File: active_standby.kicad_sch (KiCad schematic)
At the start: 13 parts, among them Q2 BSS138, U24 SN3257QDYYRQ1, U30 SN3257QDYYRQ1

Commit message: Add OTHER\_HW\_POWER\_N to a GPIO
So in the externally driven active/standby case the other power state
can be monitored.

Also fix issues in the processor pin list.

Signed-off-by: Corey Minyard <corey@minyard.net>
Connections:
- net OTHER_HW_POWER_OFF_N: now reaches Q2.3 (D), U30.12 (D4)
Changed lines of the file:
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@@
+	)
+	(junction
+		(at 130.81 148.59)
+		(diameter 0)
+		(color 0 0 0 0)
 	)
 	(junction
@@
 	(wire
 		(pts
+			(xy 130.81 148.59) (xy 135.89 148.59)
+		)
+		(stroke
+			(width 0)
+			(type default)
+		)
+	)
+	(wire
+		(pts
 			(xy 69.85 135.89) (xy 62.23 135.89)
 		)
@@
 				(hide yes)
 			)
+		)
+	)
+	(global_label "OTHER_HW_POWER_OFF_N"
+		(shape input)
+		(at 135.89 148.59 0)
+		(fields_autoplaced yes)
+		(effects
+			(font
+				(size 1.524 1.524)
+			)
+			(justify left)
+		)
+		(property "Intersheetrefs" "${INTERSHEET_REFS}"
+			(at 167.4977 148.59 0)
+			(effects
+				(font
+					(size 1.27 1.27)
+				)
+				(justify left)
+				(hide yes)
+			)

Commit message: Change a transistor to a SOT-523
Save some space

Signed-off-by: Corey Minyard <corey@minyard.net>
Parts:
- Q2: footprint Package_TO_SOT_SMD:SOT-23 -> Package_TO_SOT_SMD:SOT-523
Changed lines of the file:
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@@
 			)
 		)
-		(property "Footprint" "Package_TO_SOT_SMD:SOT-23"
+		(property "Footprint" "Package_TO_SOT_SMD:SOT-523"
 			(at 128.27 170.815 0)
 			(effects

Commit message: Convert a lot of parts to 0402
The passives across the top where things are crowded.

Signed-off-by: Corey Minyard <corey@minyard.net>
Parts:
- R101, R102, R103, R108, R113, R91, R92, R93, R94, R95: footprint Resistor_SMD:R_0603_1608Metric_Pad0.98x0.95mm_HandSolder -> Resistor_SMD:R_0402_1005Metric_Pad0.72x0.64mm_HandSolder
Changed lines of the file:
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@@
 			)
 		)
-		(property "Footprint" "Resistor_SMD:R_0603_1608Metric_Pad0.98x0.95mm_HandSolder"
+		(property "Footprint" "Resistor_SMD:R_0402_1005Metric_Pad0.72x0.64mm_HandSolder"
 			(at 236.982 73.66 90)
 			(effects
@@
 			)
 		)
-		(property "Footprint" "Resistor_SMD:R_0603_1608Metric_Pad0.98x0.95mm_HandSolder"
+		(property "Footprint" "Resistor_SMD:R_0402_1005Metric_Pad0.72x0.64mm_HandSolder"
 			(at 236.982 142.24 90)
 			(effects
@@
 			)
 		)
-		(property "Footprint" "Resistor_SMD:R_0603_1608Metric_Pad0.98x0.95mm_HandSolder"
+		(property "Footprint" "Resistor_SMD:R_0402_1005Metric_Pad0.72x0.64mm_HandSolder"
 			(at 169.672 114.3 90)
 			(effects
@@
 			)
 		)
-		(property "Footprint" "Resistor_SMD:R_0603_1608Metric_Pad0.98x0.95mm_HandSolder"
+		(property "Footprint" "Resistor_SMD:R_0402_1005Metric_Pad0.72x0.64mm_HandSolder"
 			(at 236.982 127 90)
 			(effects
@@
 			)
 		)
-		(property "Footprint" "Resistor_SMD:R_0603_1608Metric_Pad0.98x0.95mm_HandSolder"
+		(property "Footprint" "Resistor_SMD:R_0402_1005Metric_Pad0.72x0.64mm_HandSolder"
 			(at 139.192 176.53 90)
 			(effects
@@
 			)
 		)
-		(property "Footprint" "Resistor_SMD:R_0603_1608Metric_Pad0.98x0.95mm_HandSolder"
+		(property "Footprint" "Resistor_SMD:R_0402_1005Metric_Pad0.72x0.64mm_HandSolder"
 			(at 169.672 134.62 90)
 			(effects
@@
 			)
 		)
-		(property "Footprint" "Resistor_SMD:R_0603_1608Metric_Pad0.98x0.95mm_HandSolder"
+		(property "Footprint" "Resistor_SMD:R_0402_1005Metric_Pad0.72x0.64mm_HandSolder"
 			(at 132.842 33.02 90)
 			(effects
@@
 			)
 		)
-		(property "Footprint" "Resistor_SMD:R_0603_1608Metric_Pad0.98x0.95mm_HandSolder"
+		(property "Footprint" "Resistor_SMD:R_0402_1005Metric_Pad0.72x0.64mm_HandSolder"
 			(at 236.982 88.9 90)
 			(effects
@@
 			)
 		)
-		(property "Footprint" "Resistor_SMD:R_0603_1608Metric_Pad0.98x0.95mm_HandSolder"
+		(property "Footprint" "Resistor_SMD:R_0402_1005Metric_Pad0.72x0.64mm_HandSolder"
 			(at 132.842 111.76 90)
 			(effects
@@
 			)
 		)
-		(property "Footprint" "Resistor_SMD:R_0603_1608Metric_Pad0.98x0.95mm_HandSolder"
+		(property "Footprint" "Resistor_SMD:R_0402_1005Metric_Pad0.72x0.64mm_HandSolder"
 			(at 170.942 71.12 90)
 			(effects

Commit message: Add a current limiter for on-board +5V devices
Signed-off-by: Corey Minyard <corey@minyard.net>
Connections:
- net VSYS renamed +5VAL

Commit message: Update all resistors to have an ohm symbol
Make it more clean in the BOM what they are.

Signed-off-by: Corey Minyard <corey@minyard.net>
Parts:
- R101, R103, R108, R113, R91, R92, R93, R94, R95: value 10K -> 10KΩ
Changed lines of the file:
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@@
 			)
 		)
-		(property "Value" "10K"
+		(property "Value" "10KΩ"
 			(at 240.538 74.803 0)
 			(effects
@@
 			)
 		)
-		(property "Value" "10K"
+		(property "Value" "10KΩ"
 			(at 240.538 143.383 0)
 			(effects
@@
 			)
 		)
-		(property "Value" "10K"
+		(property "Value" "10KΩ"
 			(at 173.228 115.443 0)
 			(effects
@@
 			)
 		)
-		(property "Value" "10K"
+		(property "Value" "10KΩ"
 			(at 240.538 128.143 0)
 			(effects
@@
 			)
 		)
-		(property "Value" "10K"
+		(property "Value" "10KΩ"
 			(at 142.748 177.673 0)
 			(effects
@@
 			)
 		)
-		(property "Value" "10K"
+		(property "Value" "10KΩ"
 			(at 173.228 135.763 0)
 			(effects
@@
 			)
 		)
-		(property "Value" "10K"
+		(property "Value" "10KΩ"
 			(at 240.538 90.043 0)
 			(effects
@@
 			)
 		)
-		(property "Value" "10K"
+		(property "Value" "10KΩ"
 			(at 136.398 112.903 0)
 			(effects
@@
 			)
 		)
-		(property "Value" "10K"
+		(property "Value" "10KΩ"
 			(at 174.498 72.263 0)
 			(effects

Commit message: Minor fixes for BOM values
Signed-off-by: Corey Minyard <corey@minyard.net>
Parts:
- R102: value 1M -> 1MΩ
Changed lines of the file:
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@@
 			)
 		)
-		(property "Value" "1M"
+		(property "Value" "1MΩ"
 			(at 136.398 34.163 0)
 			(effects

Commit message: Added some docs and notes about various things
Signed-off-by: Corey Minyard <corey@minyard.net>
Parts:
- R91, R94: now left out of the parts list
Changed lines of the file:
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@@
 		(unit 1)
 		(exclude_from_sim no)
-		(in_bom yes)
+		(in_bom no)
 		(on_board yes)
 		(dnp yes)
@@
 		(unit 1)
 		(exclude_from_sim no)
-		(in_bom yes)
+		(in_bom no)
 		(on_board yes)
 		(dnp yes)

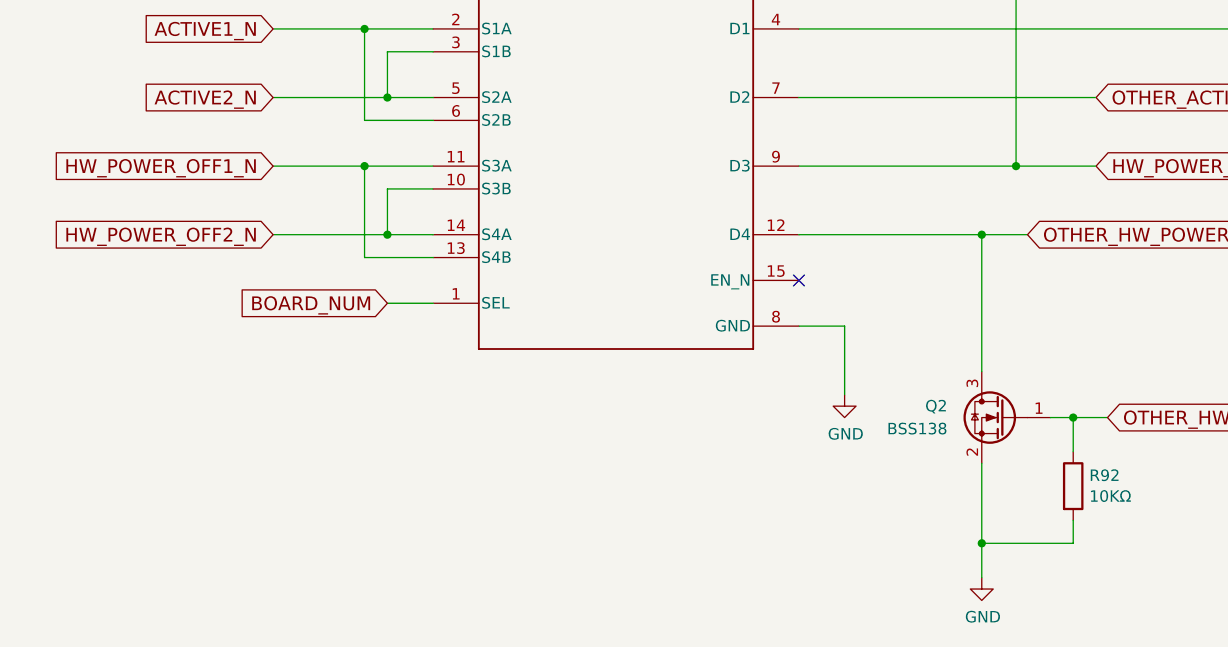
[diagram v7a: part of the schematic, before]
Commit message: Add more infromation about configuration
And add a zero-ohm resistor for bypassing the power off pin.

Signed-off-by: Corey Minyard <corey@minyard.net>
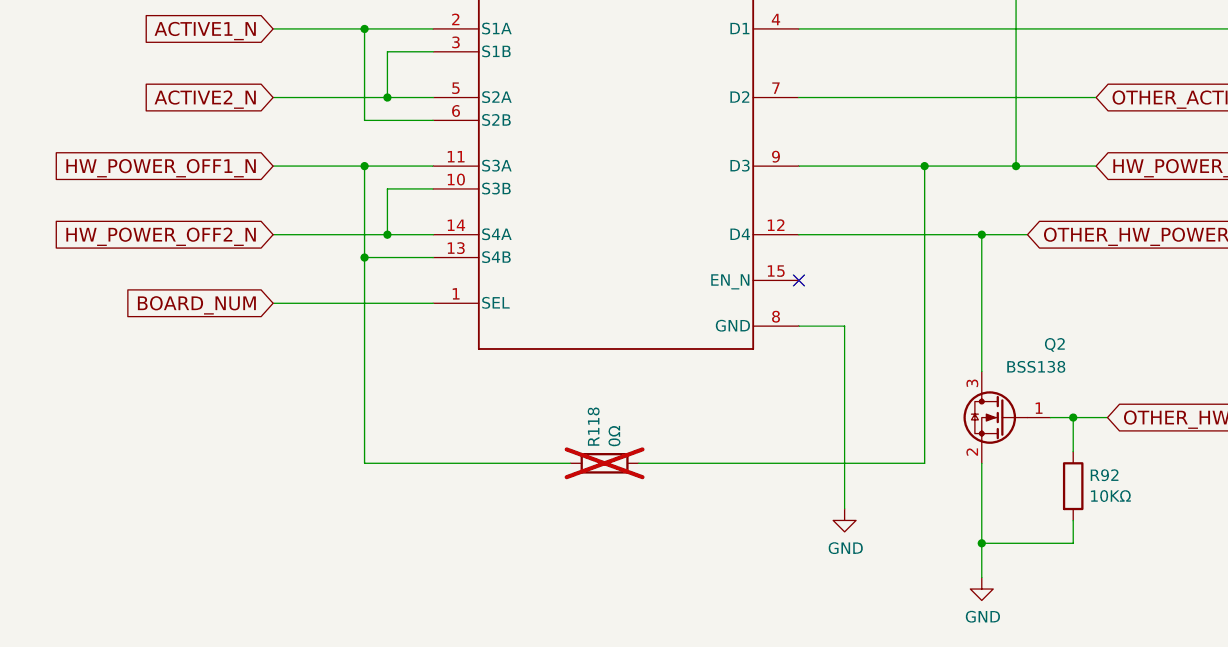
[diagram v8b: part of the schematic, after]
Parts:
- added R118: 0Ω, Resistor_SMD:R_0402_1005Metric_Pad0.72x0.64mm_HandSolder, symbol Device:R
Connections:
- net HW_POWER_OFF1_N: now also R118.1
- net HW_POWER_OFF_N: now also R118.2
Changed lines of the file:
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@@
+	)
+	(junction
+		(at 62.23 151.13)
+		(diameter 0)
+		(color 0 0 0 0)
 	)
 	(junction
@@
 	)
 	(junction
+		(at 124.46 140.97)
+		(diameter 0)
+		(color 0 0 0 0)
+	)
+	(junction
 		(at 238.76 81.28)
 		(diameter 0)
@@
 	(wire
 		(pts
-			(xy 115.57 166.37) (xy 115.57 158.75)
+			(xy 124.46 140.97) (xy 134.62 140.97)
+		)
+		(stroke
+			(width 0)
+			(type default)
+		)
+	)
+	(wire
+		(pts
+			(xy 115.57 179.07) (xy 115.57 158.75)
 		)
 		(stroke
@@
 	(wire
 		(pts
+			(xy 85.09 173.99) (xy 62.23 173.99)
+		)
+		(stroke
+			(width 0)
+			(type default)
+		)
+	)
+	(wire
+		(pts
 			(xy 140.97 182.88) (xy 130.81 182.88)
 		)
@@
 	(wire
 		(pts
-			(xy 64.77 156.21) (xy 69.85 156.21)
+			(xy 52.07 156.21) (xy 69.85 156.21)
 		)
 		(stroke
@@
 	(wire
 		(pts
+			(xy 124.46 173.99) (xy 124.46 140.97)
+		)
+		(stroke
+			(width 0)
+			(type default)
+		)
+	)
+	(wire
+		(pts
 			(xy 134.62 36.83) (xy 134.62 69.85)
 		)
@@
 	(wire
 		(pts
-			(xy 110.49 140.97) (xy 134.62 140.97)
+			(xy 110.49 140.97) (xy 124.46 140.97)
 		)
 		(stroke
@@
 	(wire
 		(pts
+			(xy 92.71 173.99) (xy 124.46 173.99)
+		)
+		(stroke
+			(width 0)
+			(type default)
+		)
+	)
+	(wire
+		(pts
 			(xy 63.5 64.77) (xy 63.5 69.85)
 		)
@@
 		(pts
 			(xy 171.45 138.43) (xy 171.45 142.24)
+		)
+		(stroke
+			(width 0)
+			(type default)
+		)
+	)
+	(wire
+		(pts
+			(xy 62.23 173.99) (xy 62.23 151.13)
 		)
 		(stroke
@@
 	(global_label "BOARD_NUM"
 		(shape input)
-		(at 64.77 156.21 180)
+		(at 52.07 156.21 180)
 		(fields_autoplaced yes)
 		(effects
@@
 		)
 		(property "Intersheetrefs" "${INTERSHEET_REFS}"
-			(at 48.4023 156.21 0)
+			(at 35.7023 156.21 0)
 			(effects
 				(font
@@
 				(justify left)
 				(hide yes)
+			)
+		)
+	)
+	(symbol
+		(lib_id "Device:R")
+		(at 88.9 173.99 90)
+		(unit 1)
+		(exclude_from_sim no)
+		(in_bom no)
+		(on_board yes)
+		(dnp yes)
+		(property "Reference" "R118"
+			(at 87.7316 172.212 0)
+			(effects
+				(font
+					(size 1.27 1.27)
+				)
+				(justify left)
+			)
+		)
+		(property "Value" "0Ω"
+			(at 90.043 172.212 0)
+			(effects
+				(font
+					(size 1.27 1.27)
+				)
+				(justify left)
+			)
+		)
+		(property "Footprint" "Resistor_SMD:R_0402_1005Metric_Pad0.72x0.64mm_HandSolder"
+			(at 88.9 175.768 90)
+			(effects
+				(font
+					(size 1.27 1.27)
+				)
+				(hide yes)
+			)
+		)
+		(property "Datasheet" "~"
+			(at 88.9 173.99 0)
+			(effects
+				(font
+					(size 1.27 1.27)
+				)
+				(hide yes)
+			)
+		)
+		(property "Description" ""
+			(at 88.9 173.99 0)
+			(effects
+				(font
+					(size 1.27 1.27)
+				)
+			)
+		)
+		(pin "1"
+		)
+		(pin "2"
+		)
+		(instances
+			(project "PacSat_AFSK"
+				(path "/cc9f42d2-6985-41ac-acab-5ab7b01c5b38/4fa888af-703c-49ed-93bb-d56d2f02c470"
+					(reference "R118")
+					(unit 1)
+				)
 			)
 		)
@@
 		(on_board yes)
 		(dnp no)
-		(fields_autoplaced yes)
 		(property "Reference" "Q2"
-			(at 127 167.6399 0)
+			(at 140.208 160.782 0)
 			(effects
 				(font
@@
 		)
 		(property "Value" "BSS138"
-			(at 127 170.1799 0)
+			(at 140.208 163.322 0)
 			(effects
 				(font
@@
 	(symbol
 		(lib_id "power:GND")
-		(at 115.57 166.37 0)
+		(at 115.57 179.07 0)
 		(unit 1)
 		(exclude_from_sim no)
@@
 		(dnp no)
 		(property "Reference" "#PWR0270"
-			(at 115.57 172.72 0)
+			(at 115.57 185.42 0)
 			(effects
 				(font
@@
 		)
 		(property "Value" "GND"
-			(at 115.697 170.7642 0)
+			(at 115.697 183.4642 0)
 			(effects
 				(font
@@
 		)
 		(property "Footprint" ""
-			(at 115.57 166.37 0)
+			(at 115.57 179.07 0)
 			(effects
 				(font
@@
 		)
 		(property "Datasheet" ""
-			(at 115.57 166.37 0)
+			(at 115.57 179.07 0)
 			(effects
 				(font
@@
 		)
 		(property "Description" ""
-			(at 115.57 166.37 0)
-			(effects
-				(font
+			(at 115.57 179.07 0)
+			(effects
+				(font
